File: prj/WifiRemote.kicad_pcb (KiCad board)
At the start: 2 copper layers, 40 x 75 mm, 68 parts, among them J1 DIP-BLACK-MALE-HEADER-VERT_4P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, J2 DIP-BLACK-MALE-HEADER_6P-2.54_, K1 DIP-SWITCH-TACTILE-SPST-NO_TS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, K2 DIP-SWITCH-TACTILE-SPST-NO_TS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, K3 DIP-SWITCH-TACTILE-SPST-NO_TS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, K4 DIP-SWITCH-TACTILE-SPST-NO_TS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, M1 Mechanical_Mount, M2 Mechanical_Mount, M3 Mechanical_Mount, M4 Mechanical_Mount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

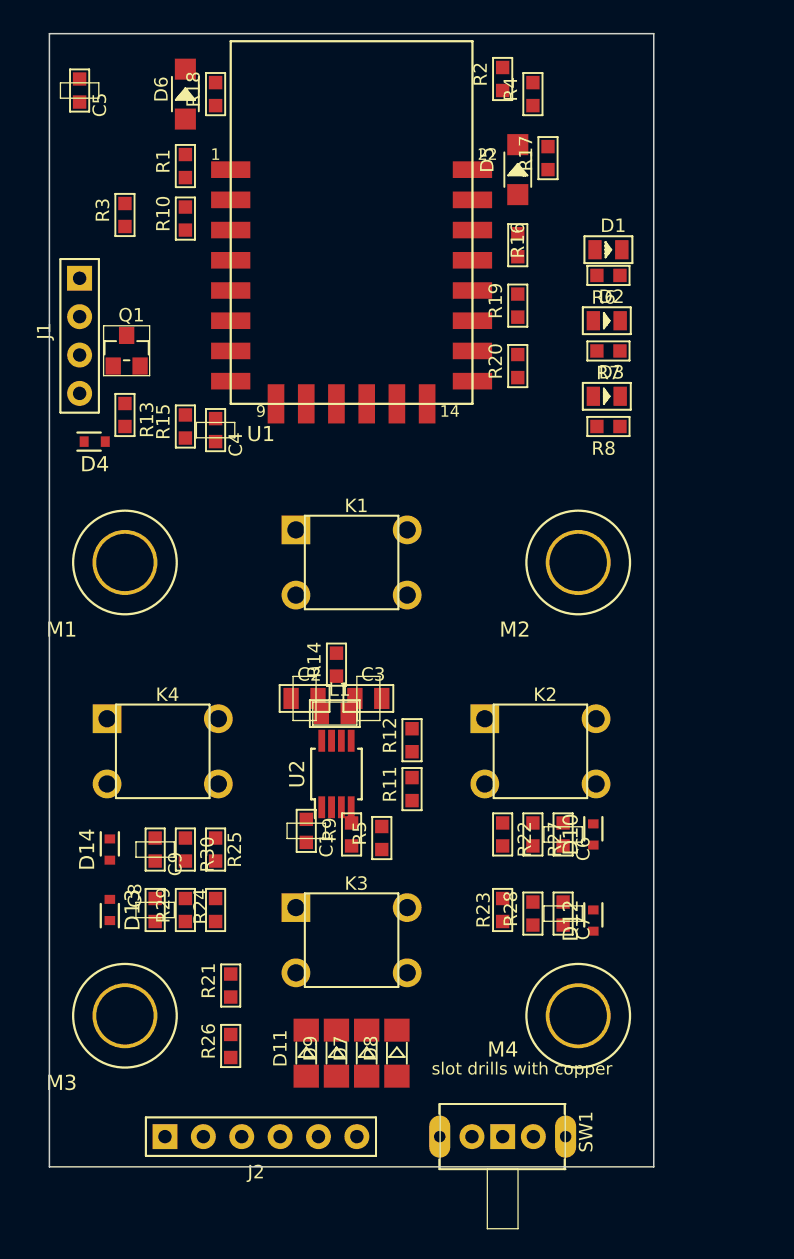
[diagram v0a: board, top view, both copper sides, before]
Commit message: Finished component layout of regulator
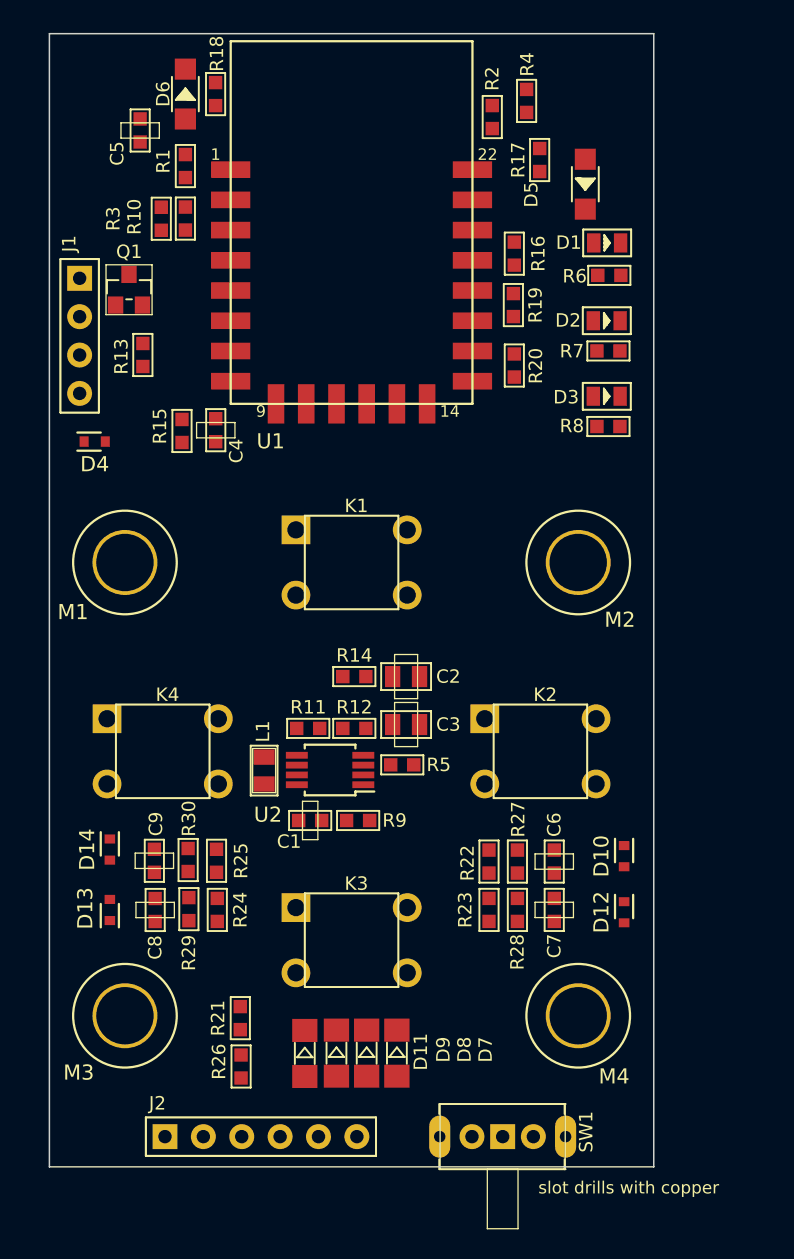
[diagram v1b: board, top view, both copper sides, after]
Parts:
- moved R11 7.96 mm to (67.1, 121.0), turned to 90 degrees
- moved C2 6.87 mm to (73.6, 117.6)
- moved L1 6.01 mm to (64.2, 123.8), turned to 90 degrees
- moved R5 5.03 mm to (73.4, 123.4), turned to 90 degrees
- moved C5 4.80 mm to (56.0, 81.4)
- moved D5 4.57 mm to (85.5, 85.0), turned to 270 degrees
- moved R13 4.14 mm to (56.2, 96.3)
- moved Q1 4.04 mm to (55.3, 91.9)
- moved R12 3.90 mm to (70.2, 121.0), turned to 270 degrees
- moved C3 3.04 mm to (73.6, 120.7)
- moved R2 2.61 mm to (79.3, 80.5)
- moved D10 2.49 mm to (88.0, 129.4)
- moved R3 2.42 mm to (57.4, 87.2)
- moved R21 2.25 mm to (62.6, 140.2), turned to 180 degrees
- moved D12 2.11 mm to (88.0, 133.1)
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
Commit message: Swapped J1 header (Battery) and J2 header (Programming)
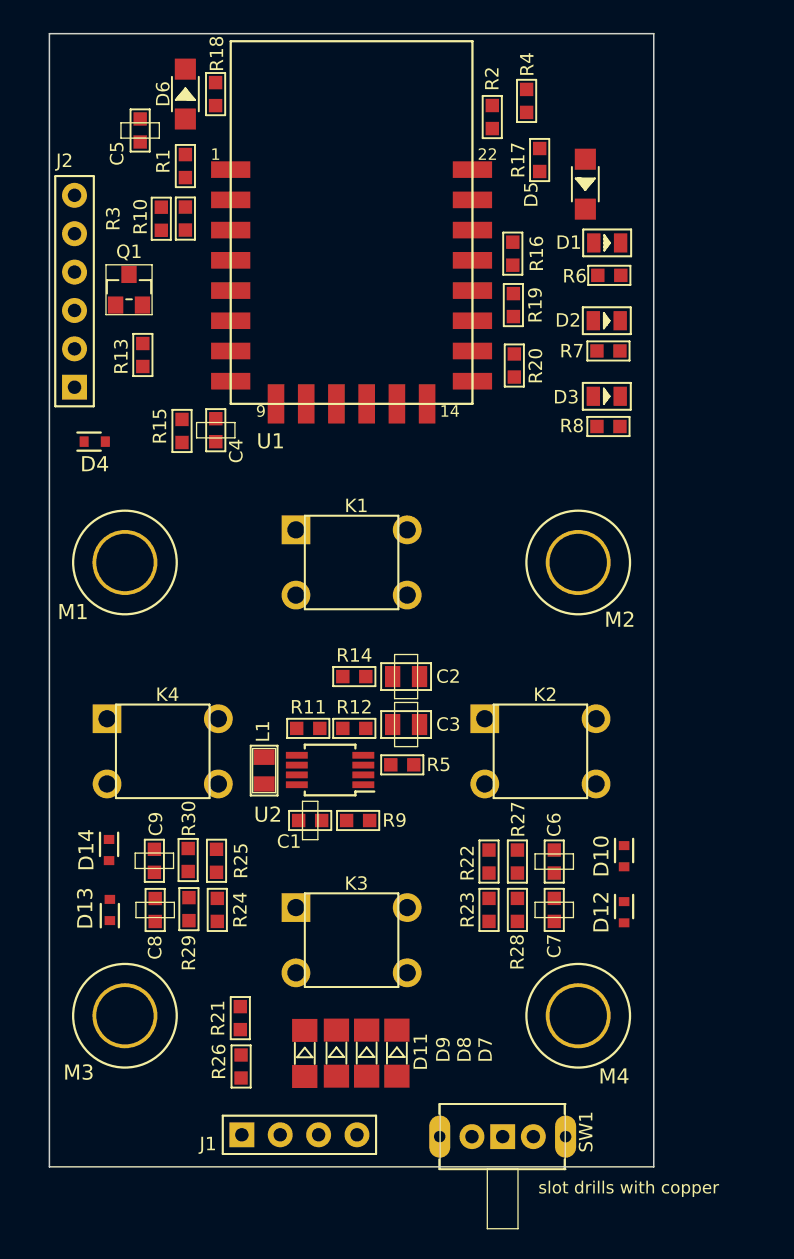
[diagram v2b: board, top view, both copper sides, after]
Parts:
- moved J2 57.3 mm to (51.7, 92.0), turned to 180 degrees
- moved J1 54.8 mm to (66.5, 147.9), turned to 90 degrees
- moved R16 0.10 mm to (80.7, 89.6)
- moved D14 0.06 mm to (53.9, 129.0)
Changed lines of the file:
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@@
   )
   (module SeeedOPL-Connector-2016:H4-2.54 (layer F.Cu)
-    (at 52 95)
+    (at 66.548 147.8788 90)
     (attr virtual)
-    (fp_text reference J1 (at -0.692 -6.1 90) (layer F.SilkS)
-      (effects (font (size 0.889 0.889) (thickness 0.1016)))
-    )
-    (fp_text value DIP-BLACK-MALE-HEADER-VERT_4P-2.54_ (at 2.0955 -0.762 90) (layer F.SilkS) hide
+    (fp_text reference J1 (at -0.6096 -6.0452 180) (layer F.SilkS)
+      (effects (font (size 0.889 0.889) (thickness 0.1016)))
+    )
+    (fp_text value DIP-BLACK-MALE-HEADER-VERT_4P-2.54_ (at 2.0955 -0.762 180) (layer F.SilkS) hide
       (effects (font (size 0.889 0.889) (thickness 0.1016)))
     )
@@
     (fp_line (start 1.27 5.08) (end -1.27 5.08) (layer F.SilkS) (width 0))
     (fp_line (start -1.27 5.08) (end -1.27 -5.08) (layer F.SilkS) (width 0))
-    (pad 1 thru_hole rect (at 0 -3.81) (size 1.651 1.651) (drill 0.889) (layers *.Cu *.Paste *.Mask)
-      (net 4 GNDD))
-    (pad 2 thru_hole circle (at 0 -1.27) (size 1.651 1.651) (drill 0.889) (layers *.Cu *.Paste *.Mask)
-      (net 4 GNDD))
-    (pad 3 thru_hole circle (at 0 1.27) (size 1.651 1.651) (drill 0.889) (layers *.Cu *.Paste *.Mask)
+    (pad 1 thru_hole rect (at 0 -3.81 90) (size 1.651 1.651) (drill 0.889) (layers *.Cu *.Paste *.Mask)
+      (net 4 GNDD))
+    (pad 2 thru_hole circle (at 0 -1.27 90) (size 1.651 1.651) (drill 0.889) (layers *.Cu *.Paste *.Mask)
+      (net 4 GNDD))
+    (pad 3 thru_hole circle (at 0 1.27 90) (size 1.651 1.651) (drill 0.889) (layers *.Cu *.Paste *.Mask)
       (net 15 +BATT))
-    (pad 4 thru_hole circle (at 0 3.81) (size 1.651 1.651) (drill 0.889) (layers *.Cu *.Paste *.Mask)
+    (pad 4 thru_hole circle (at 0 3.81 90) (size 1.651 1.651) (drill 0.889) (layers *.Cu *.Paste *.Mask)
       (net 15 +BATT))
   )
   (module SeeedOPL-Connector-2016:H6-2.54 (layer F.Cu)
-    (at 64 148 90)
+    (at 51.6636 92.0496 180)
     (attr virtual)
-    (fp_text reference J2 (at 2.204 -6.85 180) (layer F.SilkS)
-      (effects (font (size 0.889 0.889) (thickness 0.1016)))
-    )
-    (fp_text value DIP-BLACK-MALE-HEADER_6P-2.54_ (at 2.0955 -0.762 180) (layer F.SilkS) hide
+    (fp_text reference J2 (at 0.6604 8.636 360) (layer F.SilkS)
+      (effects (font (size 0.889 0.889) (thickness 0.1016)))
+    )
+    (fp_text value DIP-BLACK-MALE-HEADER_6P-2.54_ (at 2.0955 -0.762 270) (layer F.SilkS) hide
       (effects (font (size 0.889 0.889) (thickness 0.1016)))
     )
@@
     (fp_line (start 1.27 7.62) (end -1.27 7.62) (layer F.SilkS) (width 0))
     (fp_line (start -1.27 7.62) (end -1.27 -7.62) (layer F.SilkS) (width 0))
-    (pad 1 thru_hole rect (at 0 -6.35 90) (size 1.651 1.651) (drill 0.889) (layers *.Cu *.Paste *.Mask)
-      (net 4 GNDD))
-    (pad 2 thru_hole circle (at 0 -3.81 90) (size 1.651 1.651) (drill 0.889) (layers *.Cu *.Paste *.Mask)
+    (pad 1 thru_hole rect (at 0 -6.35 180) (size 1.651 1.651) (drill 0.889) (layers *.Cu *.Paste *.Mask)
+      (net 4 GNDD))
+    (pad 2 thru_hole circle (at 0 -3.81 180) (size 1.651 1.651) (drill 0.889) (layers *.Cu *.Paste *.Mask)
       (net 16 "Net-(J2-Pad2)"))
-    (pad 3 thru_hole circle (at 0 -1.27 90) (size 1.651 1.651) (drill 0.889) (layers *.Cu *.Paste *.Mask)
+    (pad 3 thru_hole circle (at 0 -1.27 180) (size 1.651 1.651) (drill 0.889) (layers *.Cu *.Paste *.Mask)
       (net 17 "Net-(J2-Pad3)"))
-    (pad 4 thru_hole circle (at 0 1.27 90) (size 1.651 1.651) (drill 0.889) (layers *.Cu *.Paste *.Mask)
+    (pad 4 thru_hole circle (at 0 1.27 180) (size 1.651 1.651) (drill 0.889) (layers *.Cu *.Paste *.Mask)
       (net 18 FTDI_TXO))
-    (pad 5 thru_hole circle (at 0 3.81 90) (size 1.651 1.651) (drill 0.889) (layers *.Cu *.Paste *.Mask)
+    (pad 5 thru_hole circle (at 0 3.81 180) (size 1.651 1.651) (drill 0.889) (layers *.Cu *.Paste *.Mask)
       (net 19 FTDI_RXI))
-    (pad 6 thru_hole circle (at 0 6.35 90) (size 1.651 1.651) (drill 0.889) (layers *.Cu *.Paste *.Mask)
+    (pad 6 thru_hole circle (at 0 6.35 180) (size 1.651 1.651) (drill 0.889) (layers *.Cu *.Paste *.Mask)
       (net 20 FTDI_DTR))
   )
@@
     (at 59 87.238)
     (attr smd)
-    (fp_text reference R10 (at -3.374 -0.116 90) (layer F.SilkS)
+    (fp_text reference R10 (at -2.9676 -0.116 90) (layer F.SilkS)
       (effects (font (size 0.889 0.889) (thickness 0.1016)))
     )
@@
   )
   (module SeeedOPL-Resistor-2016:R0603 (layer F.Cu)
-    (at 80.772 89.5604 180)
+    (at 80.6704 89.5604 180)
     (attr smd)
     (fp_text reference R16 (at -1.5875 0 270) (layer F.SilkS)
@@
     (at 79.0956 132.9944 180)
     (attr smd)
-    (fp_text reference R23 (at 1.5748 0 270) (layer F.SilkS)
+    (fp_text reference R23 (at 1.4224 0 270) (layer F.SilkS)
       (effects (font (size 0.889 0.889) (thickness 0.1016)))
     )
@@
   )
   (module Diodes_SMD:SOD-523 (layer F.Cu)
-    (at 54 129 90)
+    (at 53.9496 129.032 90)
     (descr "http://www.diodes.com/datasheets/ap02001.pdf p.144")
     (tags "Diode SOD523")

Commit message: Routing has begun
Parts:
- moved Q1 54.5 mm to (78.0, 141.5), turned to 90 degrees
- moved R13 48.1 mm to (78.2, 139.0), turned to 90 degrees
- moved D4 44.9 mm to (74.2, 141.5), turned to 270 degrees
- moved R21 18.1 mm to (77.2, 129.5)
- moved D8 14.6 mm to (79.2, 129.2)
- moved D11 14.6 mm to (60.8, 129.2)
- moved R26 11.9 mm to (62.8, 131.5), turned to 180 degrees
- moved D9 11.8 mm to (60.8, 134.0), turned to 270 degrees
- moved D7 11.7 mm to (79.2, 134.2), turned to 270 degrees
- moved R17 6.68 mm to (87.2, 88.0), turned to 270 degrees
- moved R4 6.55 mm to (81.6, 86.0), turned to 270 degrees
- moved R22 4.29 mm to (81.2, 133.5)
- moved D10 4.26 mm to (86.8, 133.5), turned to 270 degrees
- moved D5 4.25 mm to (82.5, 88.0), turned to 0 degrees
- moved R27 4.22 mm to (83.0, 133.5)
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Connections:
- SW1 pad A: +BATT -> Net-(SW1-PadA)
- SW1 pad B: Net-(SW1-PadB) -> +BATT
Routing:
- net GPIO4: track 0.00 -> 99.0 mm, vias 0 -> 2
- net GPIO5: track 0.00 -> 61.4 mm
- net GPIO12: track 0.00 -> 57.8 mm
- net GPIO13: track 0.00 -> 51.6 mm
- net GPIO14: track 0.00 -> 47.7 mm
- net FTDI_DTR: track 0.00 -> 47.1 mm
- net /SW1: track 0.00 -> 42.0 mm
- net GNDD: track 0.00 -> 40.9 mm, vias 0 -> 2
- net FTDI_TXO: track 0.00 -> 34.0 mm
- net FTDI_RXI: track 0.00 -> 33.6 mm
- net +3V3: track 0.00 -> 26.9 mm, vias 0 -> 3
- net /SW4: track 0.00 -> 21.2 mm
- net /SW2: track 0.00 -> 20.9 mm
- net GPIO2: track 0.00 -> 19.0 mm
- net /REG_IN: track 0.00 -> 16.5 mm
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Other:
- net class 15mil added: clearance 0.2, trace_width 0.3, via_dia 0.6, via_drill 0.4
- net class elephant added: clearance 0.2, trace_width 0.5, via_dia 0.6, via_drill 0.4
- net class larger added: clearance 0.2, trace_width 0.4, via_dia 0.6, via_drill 0.4

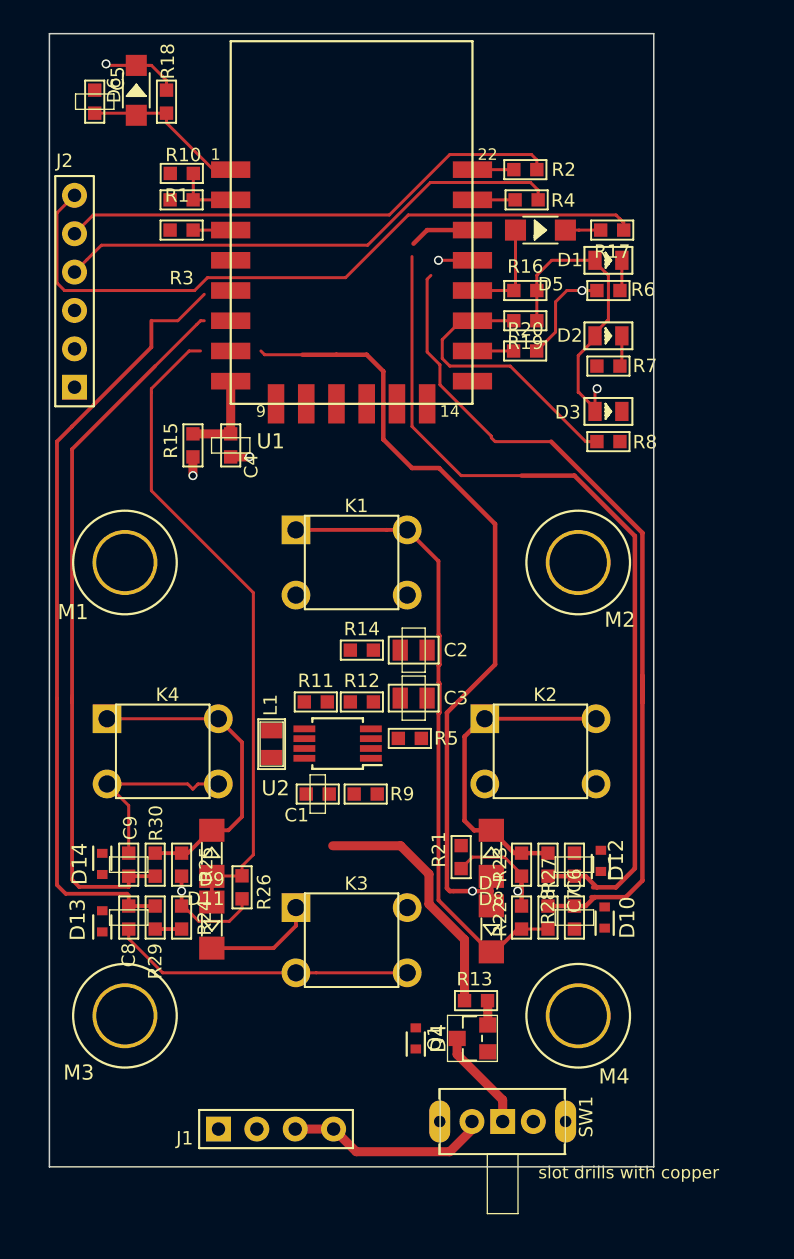
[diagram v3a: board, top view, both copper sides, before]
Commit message: Swapped LED colors, changed mechanical mounts, fixed schematic TVS diode pins, edited button connections to ESP
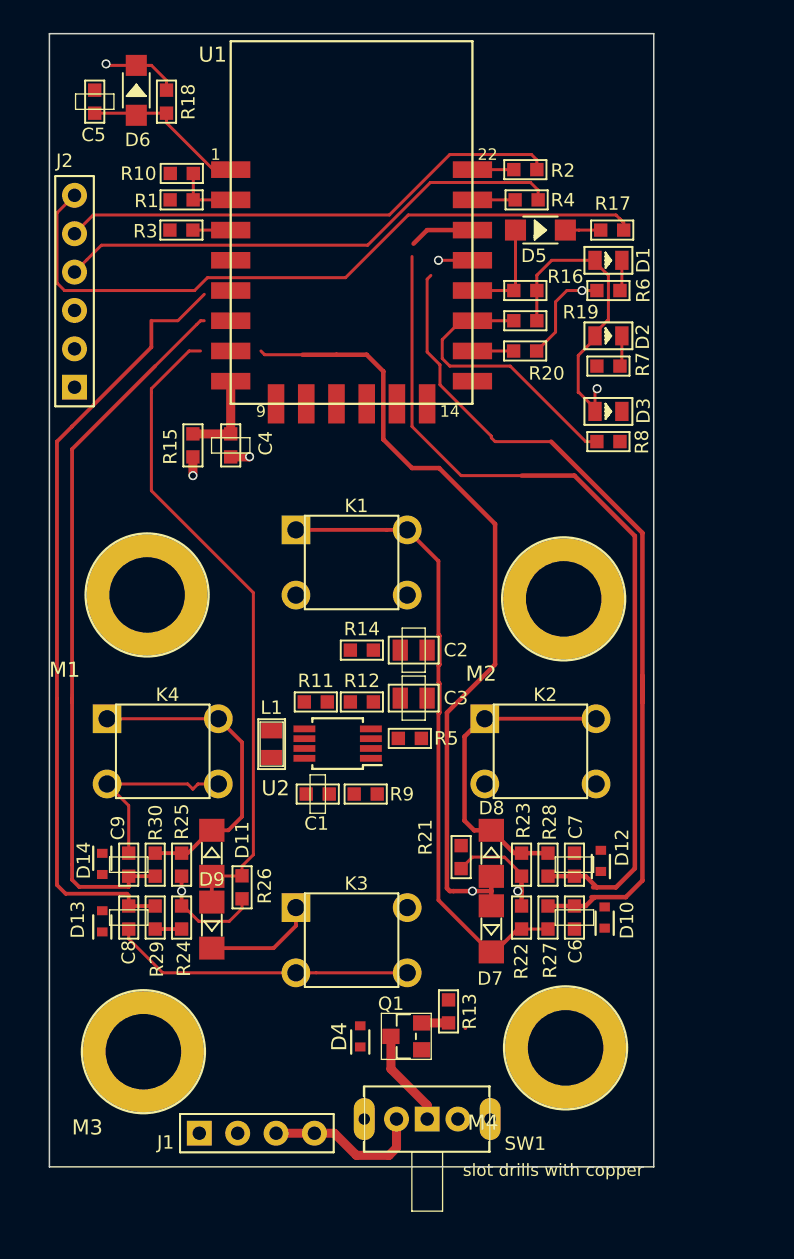
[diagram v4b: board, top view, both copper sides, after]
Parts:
- D2: value SMD-LED-CLEAR-GREEN_0805_ -> SMD-LED-CLEAR-BLUE_0805_
- M1, M2, M3, M4: footprint ICEE-Mechanical:mounting_panhead6 -> ICEE-Mechanical:mounting_panhead6_5mm
- moved SW1 5.00 mm to (75.0, 146.8)
- moved Q1 4.38 mm to (73.6, 141.4)
- moved D4 3.68 mm to (70.6, 141.4)
- moved M3 2.68 mm to (56.2, 142.4)
- moved M1 2.60 mm to (56.5, 112.1)
- moved M2 2.59 mm to (84.0, 112.4)
- moved M4 2.28 mm to (84.2, 142.1)
- moved R13 1.96 mm to (76.4, 139.7), turned to 0 degrees
- moved J1 1.30 mm to (63.7, 147.8)
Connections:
- C6 pad 2: GPIO5 -> GPIO12
- C7 pad 2: GPIO12 -> GPIO5
- R27 pad 1: GPIO5 -> GPIO12
- R28 pad 1: GPIO12 -> GPIO5
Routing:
- net (no net): track 0.00 -> 108.1 mm
- net GPIO12: track 57.8 -> 3.36 mm
- net GPIO5: track 61.4 -> 7.81 mm
- net /REG_IN: track 16.5 -> 0.00 mm
- net +BATT: track 13.5 -> 10.7 mm

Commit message: Completed routing awaiting review
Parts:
- D10, D12, D13, D14, D4: footprint Diodes_SMD:SOD-523 -> ICEE-Diode:SOD-523
- moved R21 12.6 mm to (64.8, 128.2)
- moved D4 7.43 mm to (78.0, 141.4)
- moved D10 0.25 mm to (86.5, 133.5)
- moved D12 0.25 mm to (86.5, 130.0), turned to 90 degrees
- moved D13 0.25 mm to (53.5, 133.5)
- moved D14 0.05 mm to (53.5, 130.0)
- turned C5 to 0 degrees
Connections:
- C6 pad 2: GPIO12 -> GPIO4
- C8 pad 2: GPIO13 -> GPIO14
- C9 pad 2: GPIO14 -> GPIO12
- D10 pad 1: (no net) -> GPIO4
- D10 pad 2: (no net) -> GNDD
- D11 pad A: GPIO4 -> GPIO13
- D12 pad 1: (no net) -> GPIO5
- D12 pad 2: (no net) -> GNDD
- D13 pad 1: (no net) -> GPIO14
- D13 pad 2: (no net) -> GNDD
- D14 pad 1: (no net) -> GPIO12
- D14 pad 2: (no net) -> GNDD
- D4 pad 1: (no net) -> /SWITCH_BAT
- D4 pad 2: (no net) -> GNDD
- D7 pad A: GPIO4 -> GPIO13
- D8 pad A: GPIO4 -> GPIO13
- D9 pad A: GPIO4 -> GPIO13
- M1 pad 1: (no net) -> GNDD
- M2 pad 1: (no net) -> GNDD
- M3 pad 1: (no net) -> GNDD
- M4 pad 1: (no net) -> GNDD
- R26 pad 2: GPIO4 -> GPIO13
- R27 pad 1: GPIO12 -> GPIO4
- R29 pad 1: GPIO13 -> GPIO14
- R30 pad 1: GPIO14 -> GPIO12
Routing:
- net GNDD: track 40.9 -> 360.5 mm, vias 2 -> 9
- net (no net): track 108.1 -> 0.00 mm
- net +3V3: track 26.9 -> 124.7 mm, vias 3 -> 5
- net +BATT: track 10.7 -> 108.4 mm, vias 0 -> 1
- net GPIO13: track 51.6 -> 122.9 mm
- net GPIO5: track 7.81 -> 60.4 mm
- net GPIO12: track 3.36 -> 46.9 mm
- net GPIO4: track 99.0 -> 60.6 mm, vias 2 -> 0
- net /BTN_PWR: track 14.1 -> 48.3 mm, vias 2 -> 1
- net /REG_IN: track 0.00 -> 32.2 mm
- net GPIO0: track 6.78 -> 38.2 mm, vias 0 -> 2
- net FTDI_RXI: track 33.6 -> 55.5 mm
- net /SW3: track 9.42 -> 19.3 mm
- net /3V3_OUT: track 0.00 -> 8.68 mm
- net GPIO14: track 47.7 -> 54.5 mm
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- added copper zone on B.Cu, net GNDD
- added copper zone on F.Cu, net GNDD
